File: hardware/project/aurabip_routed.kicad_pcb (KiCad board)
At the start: 4 copper layers, 52 x 52 mm, 53 parts, among them J1 USB-C, J2 AKKU, J3 SPEAKER, J4 OLED SPI, SW1 EIN/AUS, SW2 RESET, SW3 BOOT, U1 ESP32-S3-MINI-1, U10 E22-900M22S, U2 BMP581, U3 LSM6DSO32, U4 SHT40, U5 L96, U6 MAX98357A, U7 MCP73831, U8 AP2112K-3.3, U9 USBLC6

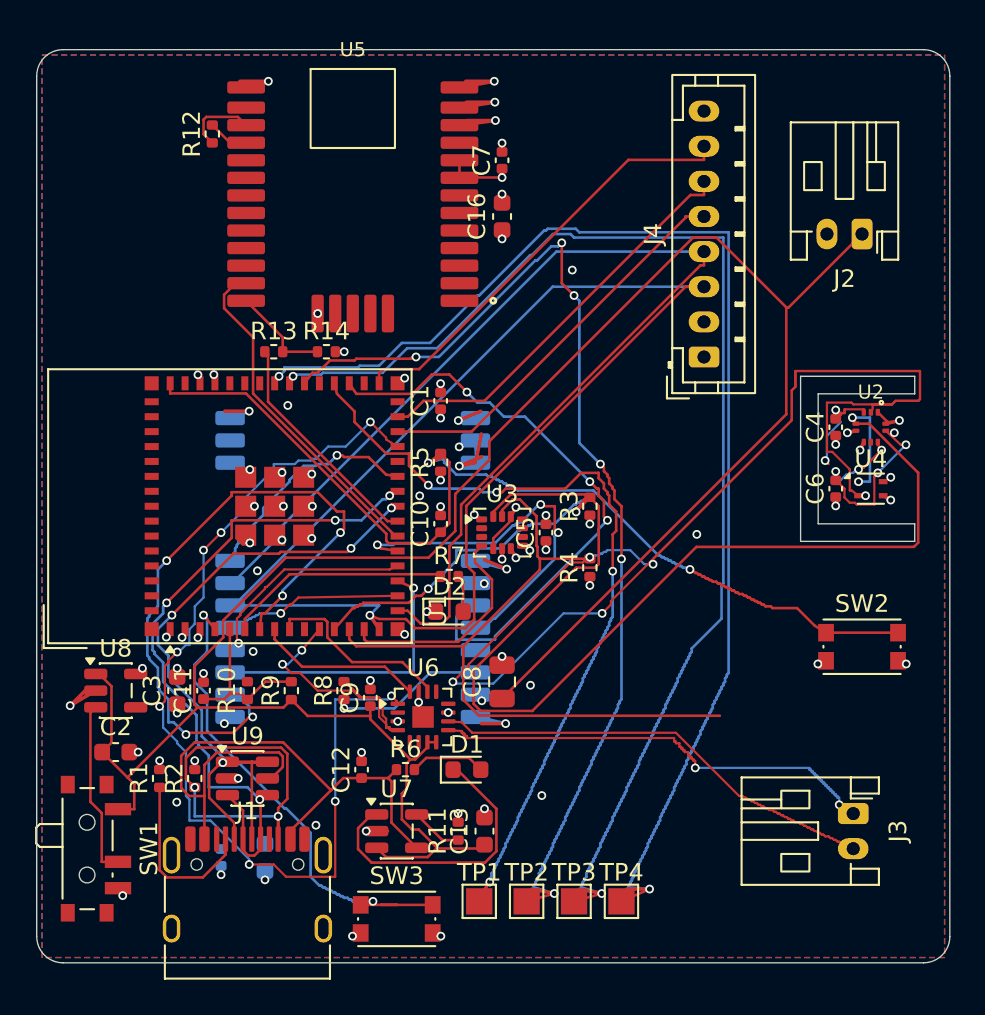
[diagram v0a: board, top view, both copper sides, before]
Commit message: wip(pcb): Via-in-Pad 10 offen - Snug-Loeser (U7.2/U9.2/U4.1/U9.4/U1.23), DRC 0/0
Co-Authored-By: Claude Fable 5 <noreply@anthropic.com>
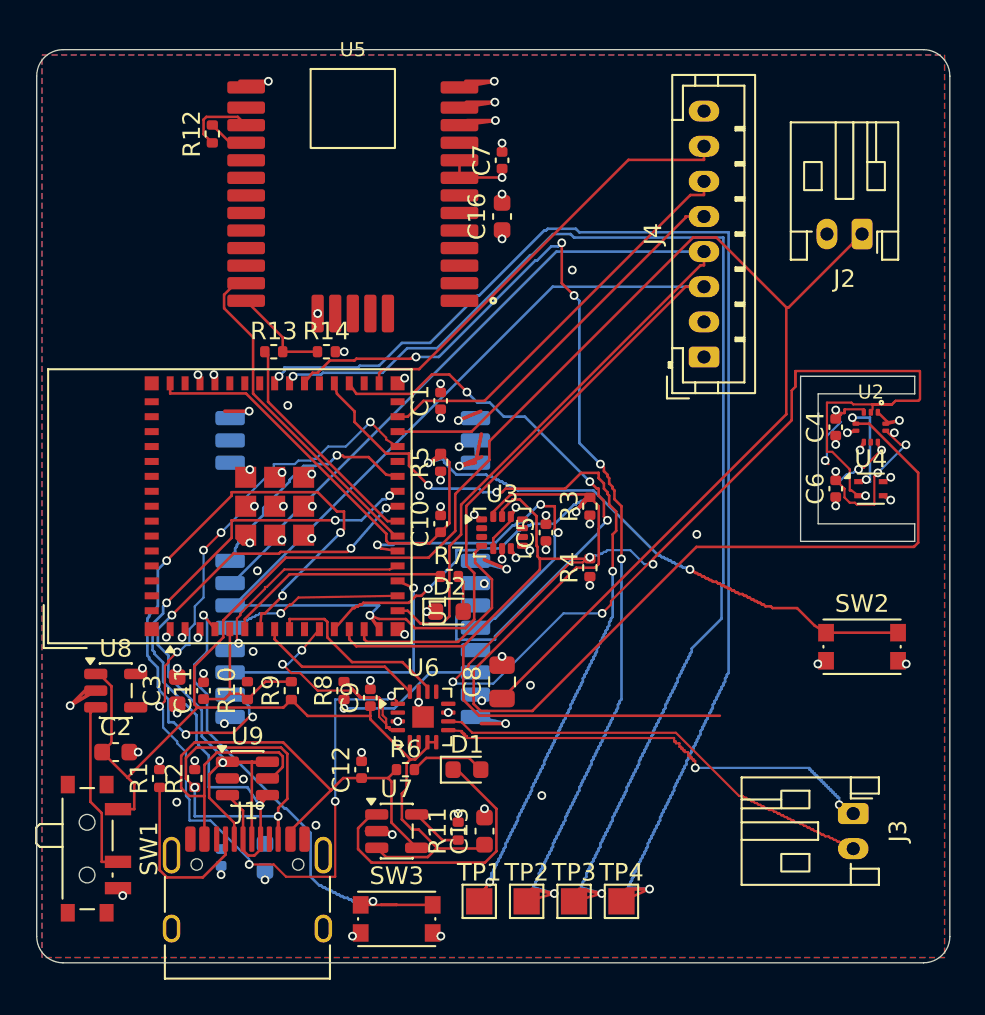
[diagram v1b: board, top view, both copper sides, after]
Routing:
- net GND: track 77.9 -> 80.9 mm
- net USB_DP: track 40.3 -> 41.4 mm
- net USB_DN: track 40.5 -> 41.1 mm
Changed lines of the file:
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@@
 	(segment
 		(start 19.975 44.5)
-		(end 18.7625 44.5)
+		(end 20.249667 44.695789)
 		(width 0.2)
 		(layer "F.Cu")
@@
 	(segment
 		(start 19.3625 44.5)
-		(end 18.7625 44.5)
+		(end 20.249667 44.695789)
 		(width 0.2)
 		(locked yes)
@@
 	(segment
 		(start 10.2625 41.5)
-		(end 11.475 41.5)
+		(end 11.772433 41.539157)
 		(width 0.2)
 		(layer "F.Cu")
@@
 	)
 	(segment
+		(start 11.012361 41.506448)
+		(end 11.772433 41.539157)
+		(width 0.2)
+		(layer "F.Cu")
+		(net "GND")
+	)
+	(segment
 		(start 44.9 23.4)
 		(end 45.1 23.6)
@@
 	)
 	(segment
+		(start 19.508975 44.532325)
+		(end 20.249667 44.695789)
+		(width 0.2)
+		(layer "F.Cu")
+		(net "GND")
+	)
+	(segment
 		(start 47.7 25.9)
 		(end 46.7 25.9)
@@
 	(segment
 		(start 10.8625 41.5)
-		(end 11.475 41.5)
+		(end 11.772433 41.539157)
 		(width 0.2)
 		(locked yes)
@@
 	)
 	(segment
-		(start 18.7625 44.5)
+		(start 20.249667 44.695789)
 		(end 18.7625 44.5)
 		(width 0.2)
@@
 	)
 	(via
-		(at 18.7625 44.5)
+		(at 20.249667 44.695789)
 		(size 0.5)
 		(drill 0.3)
@@
 	)
 	(via
-		(at 11.475 41.5)
+		(at 11.772433 41.539157)
 		(size 0.5)
 		(drill 0.3)
@@
 	)
 	(segment
+		(start 46.872444 24.580588)
+		(end 47.234666 24.483531)
+		(width 0.2)
+		(layer "F.Cu")
+		(net "I2C_SDA")
+	)
+	(segment
 		(start 31.2 25.6)
 		(end 30.716653 26.323378)
@@
 	)
 	(via
-		(at 46.8 24.6)
+		(at 47.234666 24.483531)
 		(size 0.5)
 		(drill 0.3)
@@
 	)
 	(segment
-		(start 46.8 24.6)
+		(start 47.234666 24.483531)
 		(end 47.45 24.6)
 		(width 0.15)
@@
 	)
 	(segment
+		(start 13.049124 42.571201)
+		(end 12.7 43.05)
+		(width 0.2)
+		(layer "F.Cu")
+		(net "USB_DP")
+	)
+	(segment
 		(start 11.75 45.5883)
 		(end 11.75 44.955)
@@
 	)
 	(segment
-		(start 12.7 42.7)
+		(start 12.7 43.05)
 		(end 13.1375 42.45)
 		(width 0.15)
@@
 	)
 	(via
-		(at 12.7 42.7)
+		(at 12.7 43.05)
 		(size 0.5)
 		(drill 0.3)
@@
 	(segment
 		(start 12 42)
-		(end 12.7 42.7)
+		(end 12.7 43.05)
 		(width 0.15)
 		(layer "B.Cu")
@@
 	)
 	(segment
+		(start 20.451162 26.015205)
+		(end 19.9 26.1)
+		(width 0.2)
+		(layer "F.Cu")
+		(net "USB_DN")
+	)
+	(segment
 		(start 12.25 40.55)
 		(end 10.8625 40.55)
@@
 	(segment
 		(start 20.55 26)
-		(end 20.2 26.1)
+		(end 19.9 26.1)
 		(width 0.15)
 		(layer "F.Cu")
@@
 	)
 	(via
-		(at 20.2 26.1)
+		(at 19.9 26.1)
 		(size 0.5)
 		(drill 0.3)
@@
 	)
 	(segment
-		(start 20.2 26.1)
+		(start 19.9 26.1)
 		(end 17.9 28.4)
 		(width 0.15)

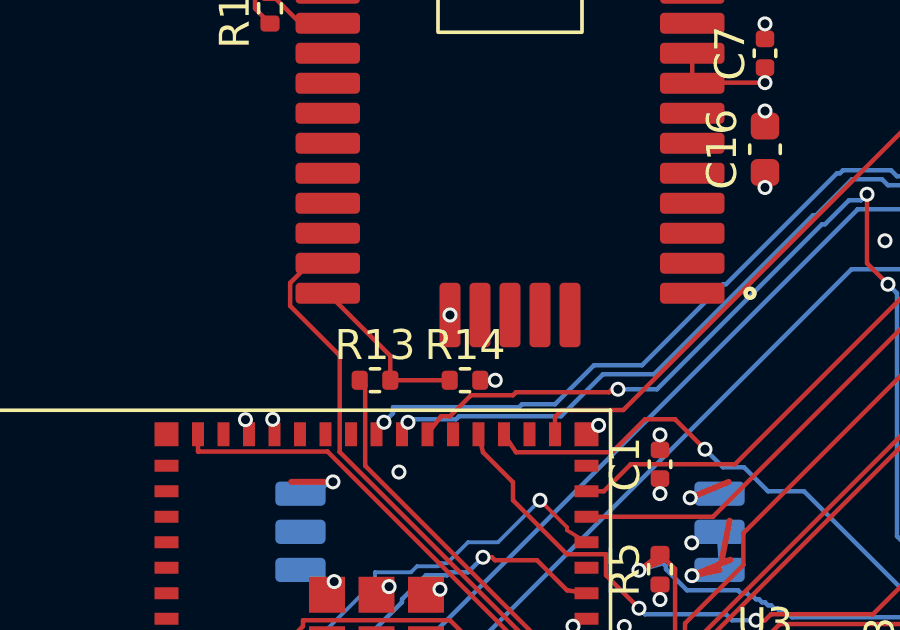
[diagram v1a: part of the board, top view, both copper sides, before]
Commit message: wip(pcb): Via-in-Pad 9 offen - U5.31 GND redundant (F-Zone deckt Pad), Via geloescht, DRC 0/0
Co-Authored-By: Claude Fable 5 <noreply@anthropic.com>
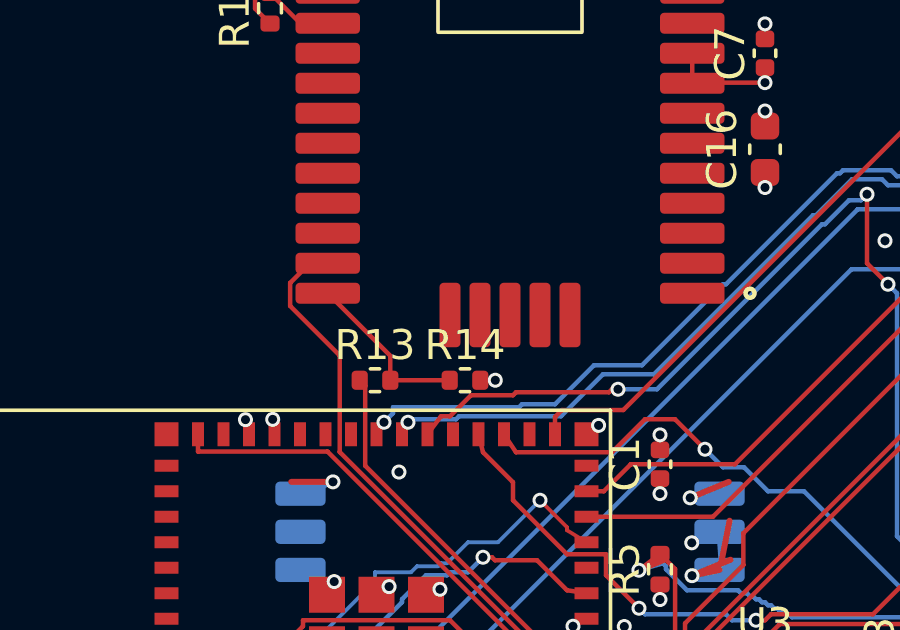
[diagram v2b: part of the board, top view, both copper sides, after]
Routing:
- net GND: vias 79 -> 78
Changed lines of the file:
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@@
-	)
-	(via
-		(at 16 15.025)
-		(size 0.5)
-		(drill 0.3)
-		(layers "F.Cu" "B.Cu")
-		(net "GND")
 	)
 	(via

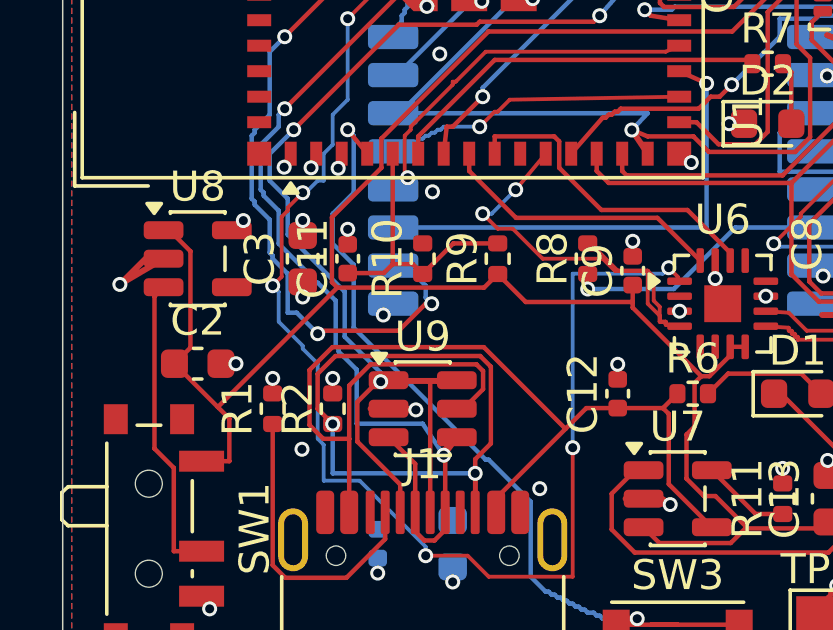
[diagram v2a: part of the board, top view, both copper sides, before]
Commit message: wip(pcb): Via-in-Pad 8 offen - U10.12 GND redundant, Via geloescht, DRC 0/0
Co-Authored-By: Claude Fable 5 <noreply@anthropic.com>
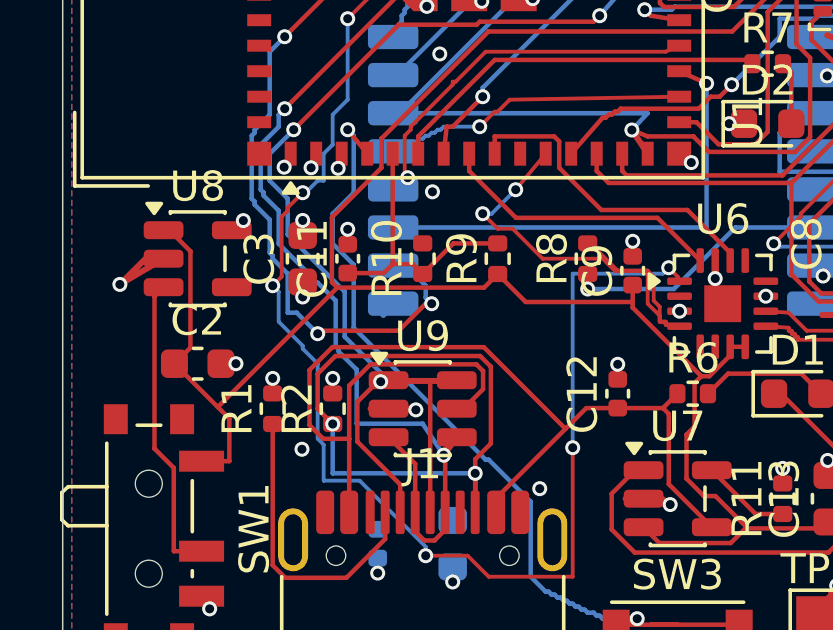
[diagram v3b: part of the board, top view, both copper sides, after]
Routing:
- net GND: vias 78 -> 77
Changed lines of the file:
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@@
-	)
-	(via
-		(at 10.686147 38.376638)
-		(size 0.5)
-		(drill 0.3)
-		(layers "F.Cu" "B.Cu")
-		(locked yes)
-		(net "GND")
 	)
 	(via

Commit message: wip(pcb): Via-in-Pad 6 offen - U10.10/U10.5 GND redundant, Vias geloescht, DRC 0/0
Co-Authored-By: Claude Fable 5 <noreply@anthropic.com>
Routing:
- net GND: vias 77 -> 75
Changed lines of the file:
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@@
-	)
-	(via
-		(at 25.484261 30.40716)
-		(size 0.5)
-		(drill 0.3)
-		(layers "F.Cu" "B.Cu")
-		(locked yes)
-		(net "GND")
 	)
 	(via
@@
 		(size 0.5)
 		(drill 0.3)
-		(layers "F.Cu" "B.Cu")
-		(locked yes)
-		(net "GND")
-	)
-	(via
-		(at 25.345064 37.076919)
-		(size 0.5)
-		(drill 0.3)

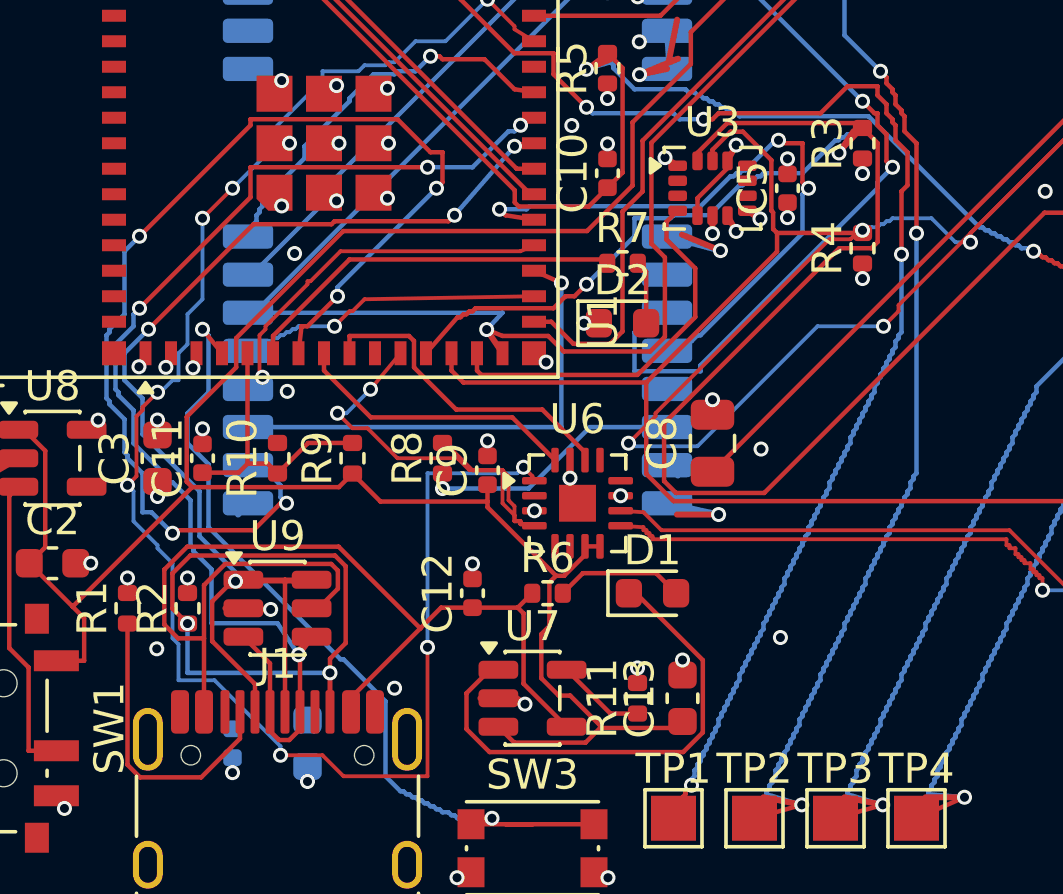
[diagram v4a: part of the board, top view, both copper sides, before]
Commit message: fix(pcb): letzte 6 Via-in-Pad weggeroutet - 0 in-pad, DRC 0/0, kein PCBWay-Fuellprozess noetig
Reste (R4.2 SCL, U9.1 USB_DN, R2.1 CC2, U6.3/U6.11/U10.15 GND) off-pad
geloest: GND per EP-Tie bzw. Off-pad-Stitch, Signal per lokalem Rip-and-
Reroute (route/local_maze.py, A* wie maze_router). R2.1-CC2-Via war redundant
(F-Pfad traegt) -> samt totem B-Zweig entfernt. Einzige In-Pad-Via: U1.61 EP.
DRC --severity-error: 0 Fehler / 0 unconnected. Fab neu exportiert.

Co-Authored-By: Claude Opus 4.8 <noreply@anthropic.com>
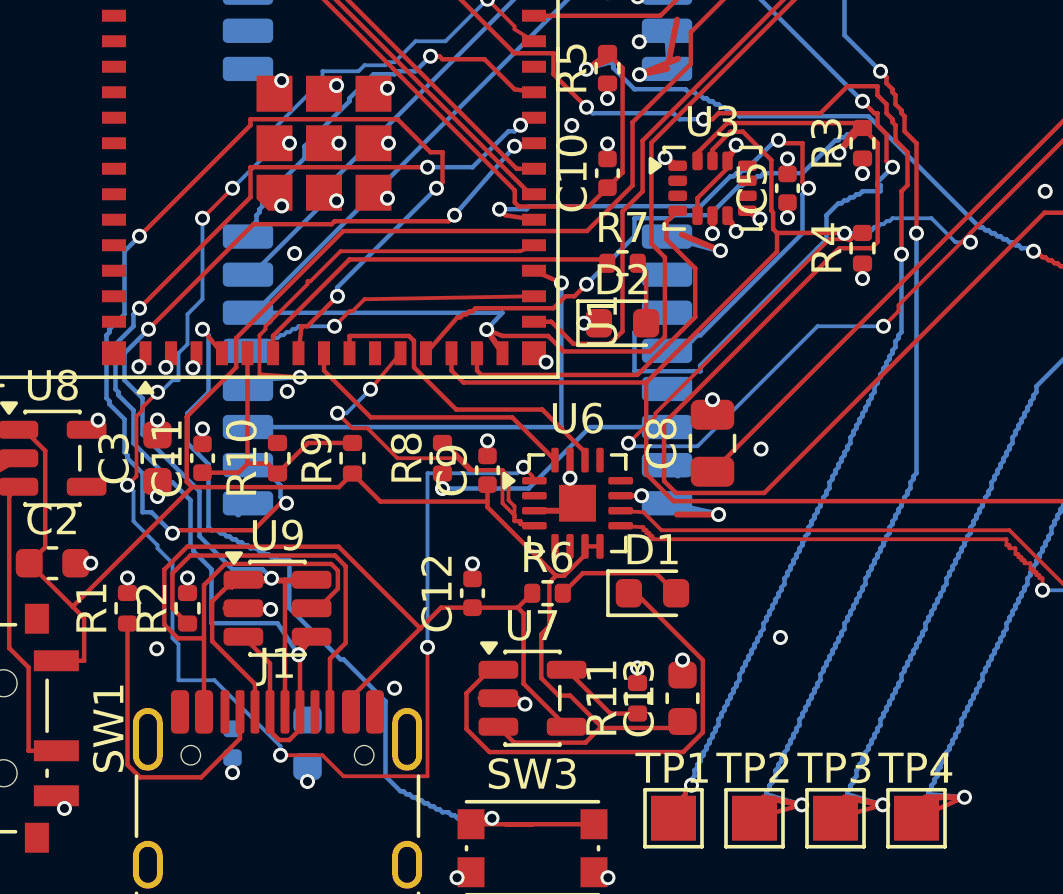
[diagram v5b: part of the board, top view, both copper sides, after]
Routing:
- net CC2: track 20.8 -> 13.1 mm, vias 2 -> 0
- net LORA_RST: track 12.5 -> 16.2 mm
- net GND: track 80.9 -> 82.6 mm, vias 75 -> 74
- net USB_DN: track 41.1 -> 42.2 mm
- net BTN_BOOT: track 30.0 -> 31.0 mm
- net LORA_RXEN: track 33.9 -> 34.6 mm
- net I2C_SCL: track 130.5 -> 131.2 mm
